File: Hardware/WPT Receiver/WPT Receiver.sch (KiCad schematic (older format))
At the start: 74 parts

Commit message: added and wired up shift registers, added debug headers, and modified pinout slightly. Cleaned up ERC and added power flags. Design passes ERC, ready to assign footprints
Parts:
- removed C?: 10uF, symbol Device:C_Small
- added C15, C21, C22, C23: 100nF, symbol Device:C_Small
- added C9: 56uF, symbol Device:CP_Small
- added D11, D13, D15, D17, D19, D21, D23, D24, D25, D26, D27, D28, D29, D30, D31, D32, D33, D34, D35, D36, D37, D38, D39, D40, D41, D42, D43, D44, D45, D46, D47, D9: RED, symbol Device:LED_ALT
- added J3: 0.1\" Header, symbol Connector:Conn_01x05_Female
- added J4: 0.1\" Header, symbol Connector:Conn_01x04_Female
- added R18, R20, R22, R25, R27, R29, R31, R33, R34, R35, R36, R37, R38, R39, R40, R41, R42, R43, R44, R45, R46, R47, R48, R49, R50, R51, R52, R53, R54, R55, R56, R57: 165, symbol Device:R_Small_US
- added TP1: TestPoint, symbol Connector:TestPoint
- added U10, U5, U8, U9: 74HC595, symbol 74xx:74HC595
- C1: renamed from C?; Voltage (none) -> 630VDC
- J1: renamed from J?; value 0.1\" header -> 0.1\" Header
- gave numbers to parts that had none: 71
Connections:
- net SER is gone; now on net SER_0: U1.18 (PA7)
- net +3V3: now also C15.1, C21.1, C22.1, C23.1, J3.1 (Pin_1), J4.1 (Pin_1), U10.16 (VCC), U5.16 (VCC), U8.16 (VCC), U9.16 (VCC); no longer D10.2 (A), D12.2 (A), D14.2 (A), D16.2 (A), D18.2 (A), D20.2 (A), D22.2 (A), D8.2 (A)
- net DEBUG_RX: now also J4.2 (Pin_2)
- net DEBUG_TX: now also J4.3 (Pin_3)
- net GND: now also R17.2, R19.2, R21.2, R24.2, R26.2, R28.2, R30.2, R32.2, C15.2, C21.2, C22.2, C23.2, C9.2, J3.5 (Pin_5), J4.4 (Pin_4), R18.2, R20.2, R22.2, R25.2, R27.2, R29.2, R31.2, R33.2, R34.2, R35.2, R36.2, R37.2, R38.2, R39.2, R40.2, R41.2, R42.2, R43.2, R44.2, R45.2, R46.2, R47.2, R48.2, R49.2, R50.2, R51.2, R52.2, R53.2, R54.2, R55.2, R56.2, R57.2, U10.8 (GND), U5.8 (GND), U8.8 (GND), U9.8 (GND)
- net HALL_INT: now also U1.38 (PD0); no longer U1.39 (PD1)
- net RCLK: now also U10.12 (RCLK), U5.12 (RCLK), U8.12 (RCLK), U9.12 (RCLK)
- net SRCLK: now also U4.11 (SRCLK), U10.11 (SRCLK), U5.11 (SRCLK), U8.11 (SRCLK), U9.11 (SRCLK)
- net SRCLR: now also U10.10 (~SRCLR), U5.10 (~SRCLR), U8.10 (~SRCLR), U9.10 (~SRCLR)
- net SR_EN: now also U10.13 (~OE), U5.13 (~OE), U8.13 (~OE), U9.13 (~OE)
- net USER_BTN1: now also C12.1, R10.2, SW2.2
- net VDC: now also C9.1
- net GPIO1: now reaches U1.42 (PB3)
- net GPIO1: now also J3.2 (Pin_2)
- net GPIO2: now reaches U1.43 (PB4)
- net GPIO2: now also J3.3 (Pin_3)
- net GPIO3: now reaches U1.44 (PB5)
- net GPIO3: now also J3.4 (Pin_4)
- net USER_BTN2: now reaches C16.1, R13.2, SW3.2
- net at U4.1 (QB): now also D20.2 (A); no longer R19.2
- net SER_0: now reaches U4.14 (SER)
- net at U4.15 (QA): now also D22.2 (A); no longer R17.2
- net at U4.2 (QC): now also D18.2 (A); no longer R21.2
- net at U4.3 (QD): now also D16.2 (A); no longer R24.2
- net at U4.4 (QE): now also D14.2 (A); no longer R26.2
- net at U4.5 (QF): now also D12.2 (A); no longer R28.2
- net at U4.6 (QG): now also D10.2 (A); no longer R30.2
- net at U4.7 (QH): now also D8.2 (A); no longer R32.2
- net SER_0-1: now reaches U4.9 (QH')
- net SER_0-1: now also U5.14 (SER)
- new net: D23.1 (K), R33.1
- new net: D23.2 (A), U5.15 (QA)
- new net: D21.1 (K), R31.1
- new net: D21.2 (A), U5.1 (QB)
- new net: D19.1 (K), R29.1
- new net: D19.2 (A), U5.2 (QC)
- new net: D17.1 (K), R27.1
- new net: D17.2 (A), U5.3 (QD)
- new net: D15.1 (K), R25.1
- new net: D15.2 (A), U5.4 (QE)
- new net: D13.1 (K), R22.1
- new net: D13.2 (A), U5.5 (QF)
- new net: D11.1 (K), R20.1
- new net: D11.2 (A), U5.6 (QG)
- new net: D9.1 (K), R18.1
- new net: D9.2 (A), U5.7 (QH)
- new net: D45.1 (K), R55.1
- new net: D45.2 (A), U8.15 (QA)
- new net: D42.1 (K), R52.1
- new net: D42.2 (A), U8.1 (QB)
- new net: D39.1 (K), R49.1
- new net: D39.2 (A), U8.2 (QC)
- new net: D36.1 (K), R46.1
- new net: D36.2 (A), U8.3 (QD)
- new net: D33.1 (K), R43.1
- new net: D33.2 (A), U8.4 (QE)
- new net: D30.1 (K), R40.1
- new net: D30.2 (A), U8.5 (QF)
- new net: D27.1 (K), R37.1
- new net: D27.2 (A), U8.6 (QG)
- new net: D24.1 (K), R34.1
- new net: D24.2 (A), U8.7 (QH)
- new net: D46.1 (K), R56.1
- new net: D46.2 (A), U9.15 (QA)
- new net: D43.1 (K), R53.1
- new net: D43.2 (A), U9.1 (QB)
- new net: D40.1 (K), R50.1
- new net: D40.2 (A), U9.2 (QC)
- new net: D37.1 (K), R47.1
- new net: D37.2 (A), U9.3 (QD)
- new net: D34.1 (K), R44.1
- new net: D34.2 (A), U9.4 (QE)
- new net: D31.1 (K), R41.1
- new net: D31.2 (A), U9.5 (QF)
- new net: D28.1 (K), R38.1
- new net: D28.2 (A), U9.6 (QG)
- new net: D25.1 (K), R35.1
- new net: D25.2 (A), U9.7 (QH)
- new net: D47.1 (K), R57.1
- new net: D47.2 (A), U10.15 (QA)
- new net: D44.1 (K), R54.1
- new net: D44.2 (A), U10.1 (QB)
- new net: D41.1 (K), R51.1
- new net: D41.2 (A), U10.2 (QC)
- new net: D38.1 (K), R48.1
- new net: D38.2 (A), U10.3 (QD)
- new net: D35.1 (K), R45.1
- new net: D35.2 (A), U10.4 (QE)
- new net: D32.1 (K), R42.1
- new net: D32.2 (A), U10.5 (QF)
- new net: D29.1 (K), R39.1
- new net: D29.2 (A), U10.6 (QG)
- new net: D26.1 (K), R36.1
- new net: D26.2 (A), U10.7 (QH)
- new net SER_1-2: U5.9 (QH'), U8.14 (SER)
- new net SER_2-3: U8.9 (QH'), U9.14 (SER)
- new net SER_3-4: U10.14 (SER), U9.9 (QH')
- new net SER_4: TP1.1, U10.9 (QH')
- no-connect marks 1 -> 24
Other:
- note added: "BUCK"
- note added: "CL = 20pF"
- note added: "CURRENT SENSE AMP"
- note added: "HALL SENSOR"
- note added: "INPUT RECTIFIER"
- note added: "MCU"
- note added: "SHIFT REGISTERS"
- note added: "TEMPERATURE SENSOR"
- note removed: "165 ohm resistor\n"
- note removed: "CL ="
- note removed: "TO DO LIST\nCreate symbol for hall sense, current sense\nImport STM32 pinout\nCreate circuits for smaller peripherals\nCreate and duplicate LED circuits\nAdd in extra headers\nThink about adding more capacitance/protection\nClean up"
- note removed: "voltage divider + zener clamp"
- moved on the sheet: C12, C14, C16, C19, C20, D10, D12, D14, D16, D18, D20, D22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

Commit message: Added footprint associations, as well as a few MPN/VDC parameters and an RC filter footprint on current sense line. Imported footprints into pcb
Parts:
- added C24: 100nF, Capacitor_SMD:C_0402_1005Metric, symbol Device:C_Small
- added R58: 0, Resistor_SMD:R_0603_1608Metric, symbol Device:R_Small_US
- C1: footprint (none) -> Capacitor_THT:C_Rect_L7.2mm_W8.5mm_P5.00mm_FKP2_FKP2_MKS2_MKP2
- C10: footprint (none) -> Capacitor_SMD:C_0603_1608Metric; VDC (none) -> 50V
- C11, C12, C13, C14, C15, C16, C19, C2, C20, C21, C22, C23, C3, C6, C7, C8: footprint (none) -> Capacitor_SMD:C_0402_1005Metric
- C17, C18, C4, C5: footprint (none) -> Capacitor_SMD:C_0603_1608Metric
- C9: footprint (none) -> Capacitor_SMD:CP_Elec_10x10; MPN (none) -> EMVA630ADA560MJA0G; VDC (none) -> 35V
- D10, D11, D12, D13, D14, D15, D16, D17, D18, D19, D20, D21, D22, D23, D24, D25, D26, D27, D28, D29, D30, D31, D32, D33, D34, D35, D36, D37, D38, D39, D40, D41, D42, D43, D44, D45, D46, D47, D8, D9: footprint (none) -> LED_SMD:LED_0603_1608Metric_Castellated
- D5: value 3.3V -> MM3Z3V3T1G; footprint (none) -> Diode_SMD:D_SOD-323; MPN MM3Z3V3T1G -> (none); Voltage (none) -> 3.3V
- FB1: footprint (none) -> Inductor_SMD:L_0603_1608Metric
- J1: footprint (none) -> Connector_PinHeader_2.54mm:PinHeader_1x02_P2.54mm_Vertical
- J3: footprint (none) -> Connector_PinHeader_2.54mm:PinHeader_1x05_P2.54mm_Vertical
- J4: footprint (none) -> Connector_PinHeader_2.54mm:PinHeader_1x04_P2.54mm_Vertical
- L1: footprint (none) -> Connector_PinHeader_2.54mm:PinHeader_2x01_P2.54mm_Vertical
- L2: footprint (none) -> WPT_Project_Parts:744042150; MPN (none) -> 744042150
- R1, R10, R11, R12, R13, R14, R15, R16, R17, R18, R19, R2, R20, R21, R22, R23, R24, R25, R26, R27, R28, R29, R3, R30, R31, R32, R33, R34, R35, R36, R37, R38, R39, R4, R40, R41, R42, R43, R44, R45, R46, R47, R48, R49, R5, R50, R51, R52, R53, R54, R55, R56, R57, R6, R7, R9: footprint (none) -> Resistor_SMD:R_0603_1608Metric
- R8: footprint (none) -> Resistor_SMD:R_1206_3216Metric
- SW1, SW2, SW3: footprint MyParts:PTS647 -> WPT_Project_Parts:PTS647
- TP1: footprint (none) -> TestPoint:TestPoint_Pad_2.5x2.5mm
- U10, U4, U5, U8, U9: footprint (none) -> Package_SO:SOIC-16_3.9x9.9mm_P1.27mm
- U6: footprint (none) -> Package_SO:SOIC-8_3.9x4.9mm_P1.27mm
- Y1: footprint (none) -> Crystal:Crystal_SMD_5032-2Pin_5.0x3.2mm
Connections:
- net GND: now also C24.2
- net ISENSE: now also C24.1, R58.1; no longer U2.1 (OUT)
- new net: R58.2, U2.1 (OUT)
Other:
- note added: "DOUBLE CHECK ALL FOOTPRINTS ARE ASSIGNED CORRECTLY (PACKAGES AND DIMENSIONS)"

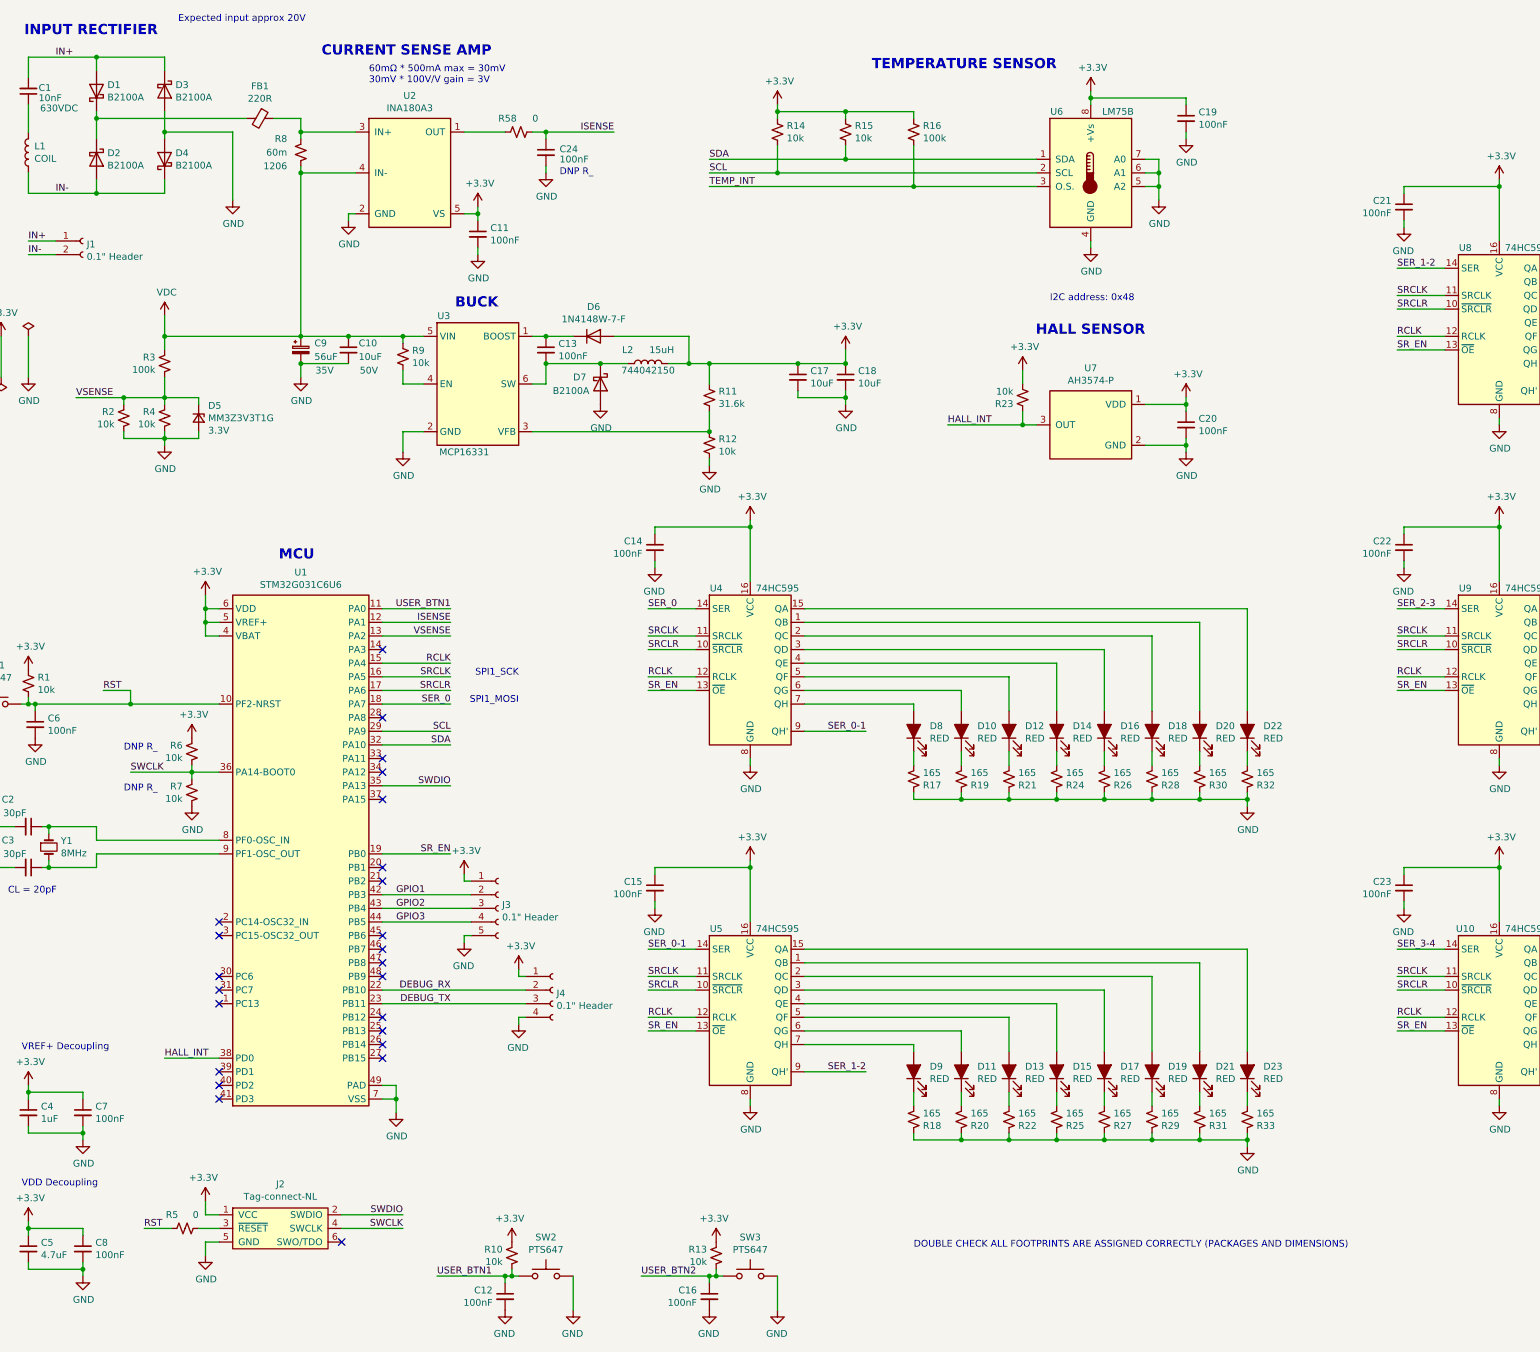
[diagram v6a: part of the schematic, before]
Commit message: Added an MPN to electrolytic caps in coil driver. Added debug LEDs to 3 pins on receiver micro
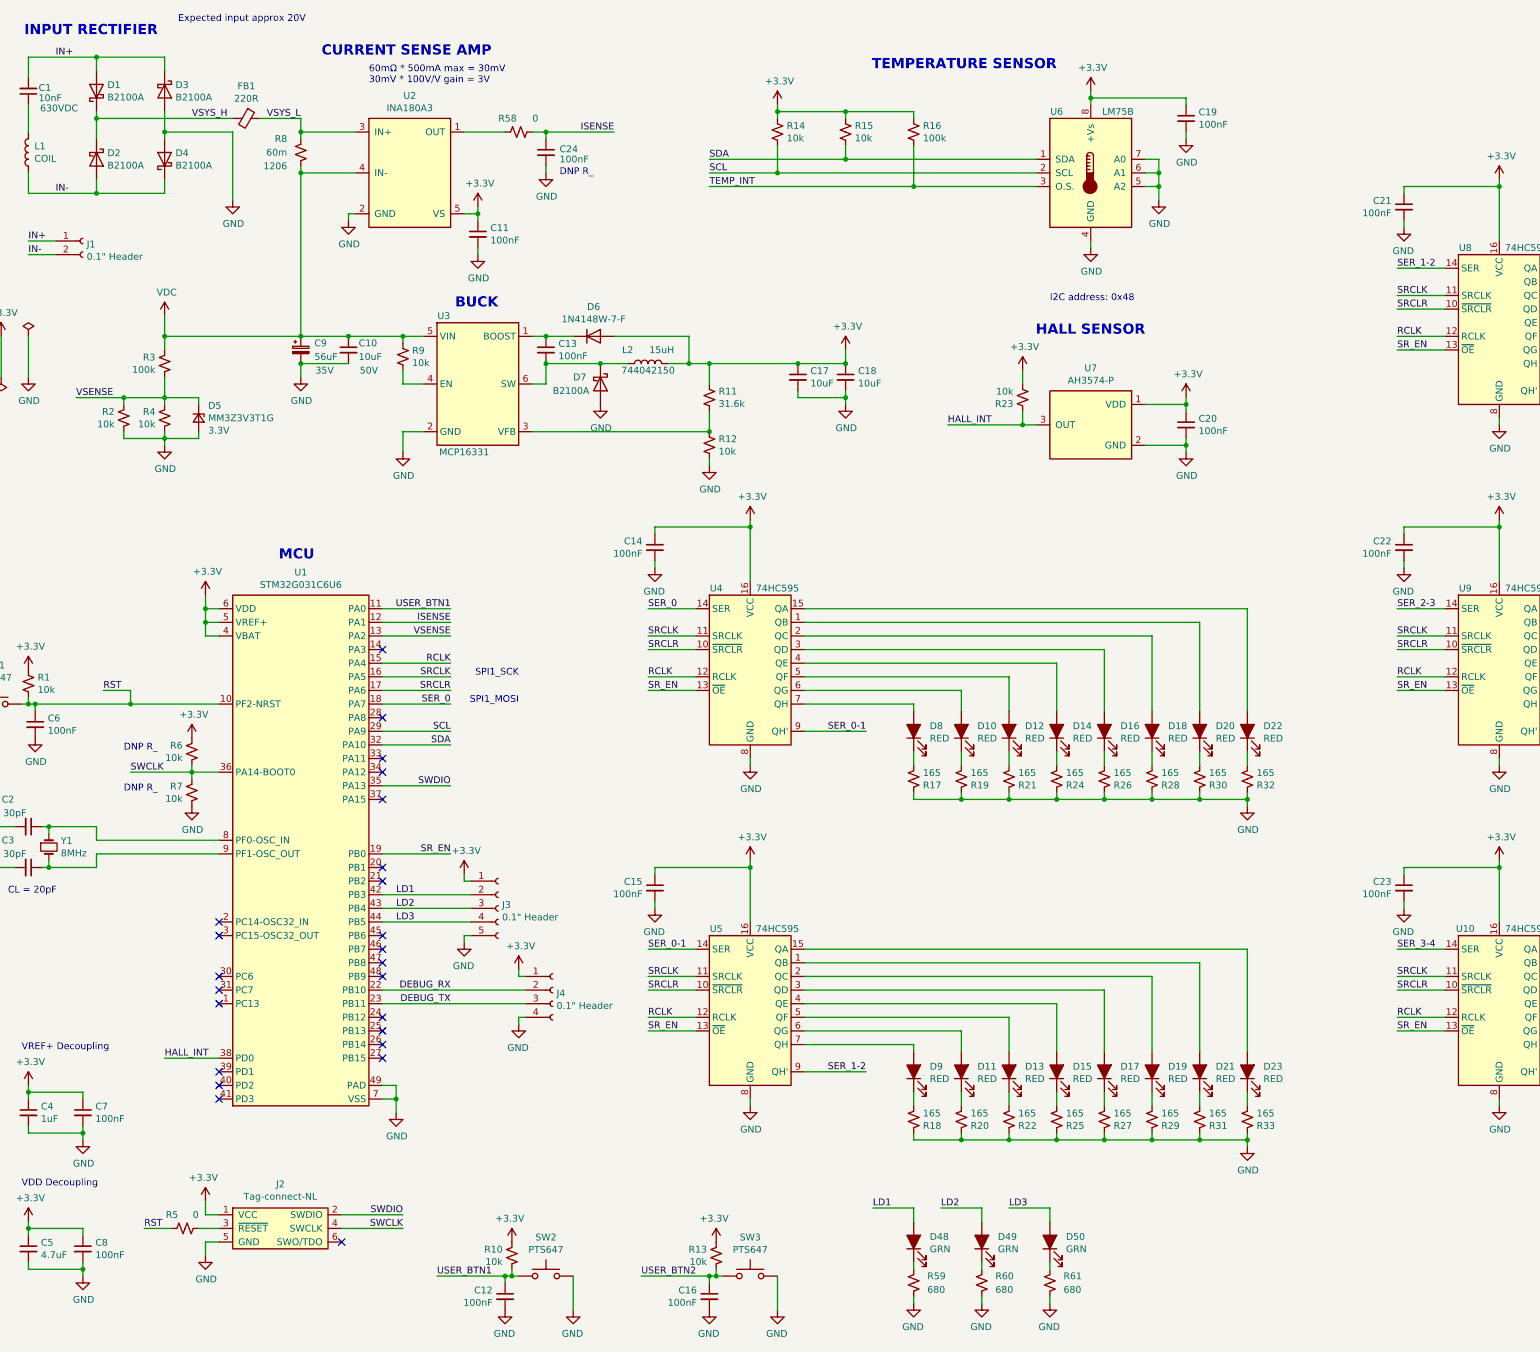
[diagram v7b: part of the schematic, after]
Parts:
- added D48, D49, D50: GRN, LED_SMD:LED_0603_1608Metric_Castellated, symbol Device:LED_ALT
- added R59, R60, R61: 680, Resistor_SMD:R_0603_1608Metric, symbol Device:R_Small_US
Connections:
- net GND: now also R59.2, R60.2, R61.2
- net VSYS_H: now reaches D1.1 (K), D2.1 (K), FB1.2
- net VSYS_L: now reaches FB1.1, R8.1, U2.3 (IN+)
- net GPIO1 renamed LD1
- net LD1: now also D48.2 (A)
- net GPIO2 renamed LD2
- net LD2: now also D49.2 (A)
- net GPIO3 renamed LD3
- net LD3: now also D50.2 (A)
- new net: D48.1 (K), R59.1
- new net: D49.1 (K), R60.1
- new net: D50.1 (K), R61.1
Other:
- note removed: "DOUBLE CHECK ALL FOOTPRINTS ARE ASSIGNED CORRECTLY (PACKAGES AND DIMENSIONS)"
- moved on the sheet: FB1
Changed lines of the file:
@@
 L Device:Ferrite_Bead_Small FB1
 U 1 1 60AF470D
-P 2700 1500
-F 0 "FB1" V 2463 1500 50  0000 C CNN
-F 1 "220R" V 2554 1500 50  0000 C CNN
-F 2 "Inductor_SMD:L_0603_1608Metric" V 2630 1500 50  0001 C CNN
-F 3 "~" H 2700 1500 50  0001 C CNN
-	1    2700 1500
+P 2600 1500
+F 0 "FB1" V 2363 1500 50  0000 C CNN
+F 1 "220R" V 2454 1500 50  0000 C CNN
+F 2 "Inductor_SMD:L_0603_1608Metric" V 2530 1500 50  0001 C CNN
+F 3 "~" H 2600 1500 50  0001 C CNN
+	1    2600 1500
 	0    1    1    0
 $EndComp
@@
 	3000 3400 3000 3300
 Wire Wire Line
-	1500 1500 2600 1500
+	1500 1500 2500 1500
 Wire Wire Line
-	2800 1500 3000 1500
+	2700 1500 3000 1500
 Wire Wire Line
 	3000 1500 3000 1600
@@
 	2000 8400 2400 8400
 Text Label 3700 7200 0    50   ~ 0
-GPIO1
+LD1
 Text Label 3700 7300 0    50   ~ 0
-GPIO2
+LD2
 Text Label 3700 7400 0    50   ~ 0
-GPIO3
+LD3
 $Comp
 L Connector:Conn_01x05_Female J3
@@
 Wire Wire Line
 	3600 8000 4650 8000
-Text Notes 7500 9800 0    50   ~ 0
-DOUBLE CHECK ALL FOOTPRINTS ARE ASSIGNED CORRECTLY (PACKAGES AND DIMENSIONS)
 $Comp
 L Device:R_Small_US R58
@@
 Text Notes 4900 1925 0    50   ~ 0
 DNP R_
+Text Label 2200 1500 0    50   ~ 0
+VSYS_H
+Text Label 2750 1500 0    50   ~ 0
+VSYS_L
+$Comp
+L Device:LED_ALT D48
+U 1 1 611BC56B
+P 7500 9750
+F 0 "D48" V 7539 9632 50  0000 R CNN
+F 1 "GRN" V 7448 9632 50  0000 R CNN
+F 2 "LED_SMD:LED_0603_1608Metric_Castellated" H 7500 9750 50  0001 C CNN
+F 3 "https://www.we-online.de/katalog/datasheet/150060VS75000.pdf" H 7500 9750 50  0001 C CNN
+F 4 "150060VS75000" V 7500 9750 50  0001 C CNN "MPN"
+	1    7500 9750
+	0    -1   -1   0
+$EndComp
+$Comp
+L Device:R_Small_US R59
+U 1 1 611BD3EF
+P 7500 10050
+F 0 "R59" H 7400 10100 50  0000 R CNN
+F 1 "680" H 7400 10000 50  0000 R CNN
+F 2 "Resistor_SMD:R_0603_1608Metric" H 7500 10050 50  0001 C CNN
+F 3 "~" H 7500 10050 50  0001 C CNN
+	1    7500 10050
+	-1   0    0    -1
+$EndComp
+$Comp
+L power:GND #PWR0104
+U 1 1 611BDBF2
+P 7500 10200
+F 0 "#PWR0104" H 7500 9950 50  0001 C CNN
+F 1 "GND" H 7505 10027 50  0000 C CNN
+F 2 "" H 7500 10200 50  0001 C CNN
+F 3 "" H 7500 10200 50  0001 C CNN
+	1    7500 10200
+	-1   0    0    -1
+$EndComp
+Wire Wire Line
+	7500 10200 7500 10150
+Wire Wire Line
+	7500 9950 7500 9900
+Text Label 7200 9500 0    50   ~ 0
+LD1
+Wire Wire Line
+	7200 9500 7500 9500
+Wire Wire Line
+	7500 9500 7500 9600
+$Comp
+L Device:LED_ALT D49
+U 1 1 612D0540
+P 8000 9750
+F 0 "D49" V 8039 9632 50  0000 R CNN
+F 1 "GRN" V 7948 9632 50  0000 R CNN
+F 2 "LED_SMD:LED_0603_1608Metric_Castellated" H 8000 9750 50  0001 C CNN
+F 3 "https://www.we-online.de/katalog/datasheet/150060VS75000.pdf" H 8000 9750 50  0001 C CNN
+F 4 "150060VS75000" V 8000 9750 50  0001 C CNN "MPN"
+	1    8000 9750
+	0    -1   -1   0
+$EndComp
+$Comp
+L Device:R_Small_US R60
+U 1 1 612D054A
+P 8000 10050
+F 0 "R60" H 7900 10100 50  0000 R CNN
+F 1 "680" H 7900 10000 50  0000 R CNN
+F 2 "Resistor_SMD:R_0603_1608Metric" H 8000 10050 50  0001 C CNN
+F 3 "~" H 8000 10050 50  0001 C CNN
+	1    8000 10050
+	-1   0    0    -1
+$EndComp
+$Comp
+L power:GND #PWR0105
+U 1 1 612D0554
+P 8000 10200
+F 0 "#PWR0105" H 8000 9950 50  0001 C CNN
+F 1 "GND" H 8005 10027 50  0000 C CNN
+F 2 "" H 8000 10200 50  0001 C CNN
+F 3 "" H 8000 10200 50  0001 C CNN
+	1    8000 10200
+	-1   0    0    -1
+$EndComp
+Wire Wire Line
+	8000 10200 8000 10150
+Wire Wire Line
+	8000 9950 8000 9900
+Text Label 7700 9500 0    50   ~ 0
+LD2
+Wire Wire Line
+	7700 9500 8000 9500
+Wire Wire Line
+	8000 9500 8000 9600
+$Comp
+L Device:LED_ALT D50
+U 1 1 6130A0B1
+P 8500 9750
+F 0 "D50" V 8539 9632 50  0000 R CNN
+F 1 "GRN" V 8448 9632 50  0000 R CNN
+F 2 "LED_SMD:LED_0603_1608Metric_Castellated" H 8500 9750 50  0001 C CNN
+F 3 "https://www.we-online.de/katalog/datasheet/150060VS75000.pdf" H 8500 9750 50  0001 C CNN
+F 4 "150060VS75000" V 8500 9750 50  0001 C CNN "MPN"
+	1    8500 9750
+	0    -1   -1   0
+$EndComp
+$Comp
+L Device:R_Small_US R61
+U 1 1 6130A0BB
+P 8500 10050
+F 0 "R61" H 8400 10100 50  0000 R CNN
+F 1 "680" H 8400 10000 50  0000 R CNN
+F 2 "Resistor_SMD:R_0603_1608Metric" H 8500 10050 50  0001 C CNN
+F 3 "~" H 8500 10050 50  0001 C CNN
+	1    8500 10050
+	-1   0    0    -1
+$EndComp
+$Comp
+L power:GND #PWR0106
+U 1 1 6130A0C5
+P 8500 10200
+F 0 "#PWR0106" H 8500 9950 50  0001 C CNN
+F 1 "GND" H 8505 10027 50  0000 C CNN
+F 2 "" H 8500 10200 50  0001 C CNN
+F 3 "" H 8500 10200 50  0001 C CNN
+	1    8500 10200
+	-1   0    0    -1
+$EndComp
+Wire Wire Line
+	8500 10200 8500 10150
+Wire Wire Line
+	8500 9950 8500 9900
+Text Label 8200 9500 0    50   ~ 0
+LD3
+Wire Wire Line
+	8200 9500 8500 9500
+Wire Wire Line
+	8500 9500 8500 9600
 $EndSCHEMATC
